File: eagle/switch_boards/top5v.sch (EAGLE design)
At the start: 9 parts

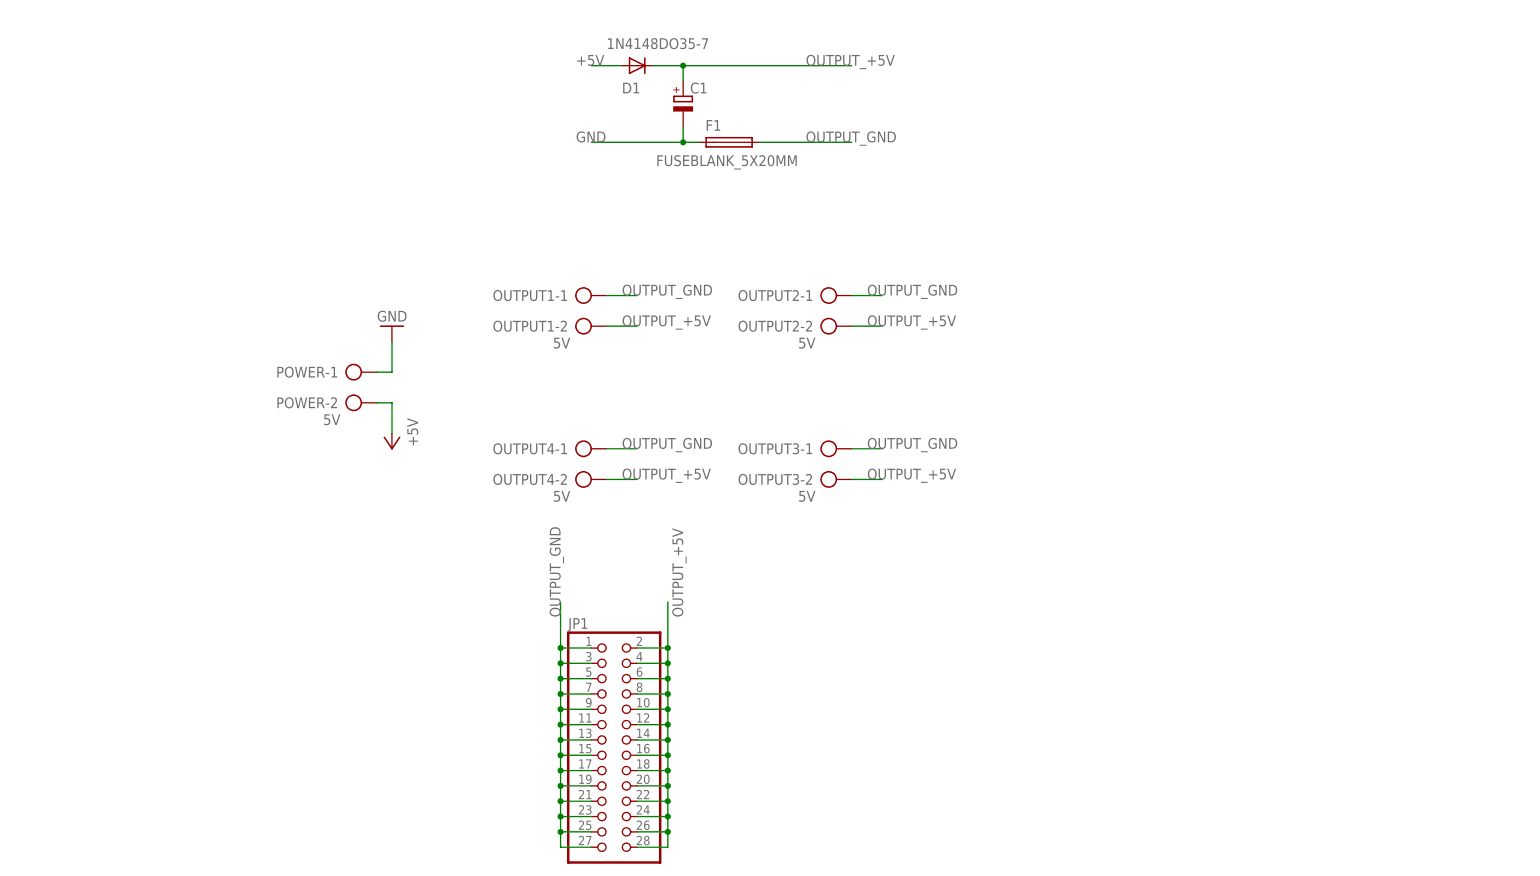
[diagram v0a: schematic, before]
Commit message: switch board for 5v
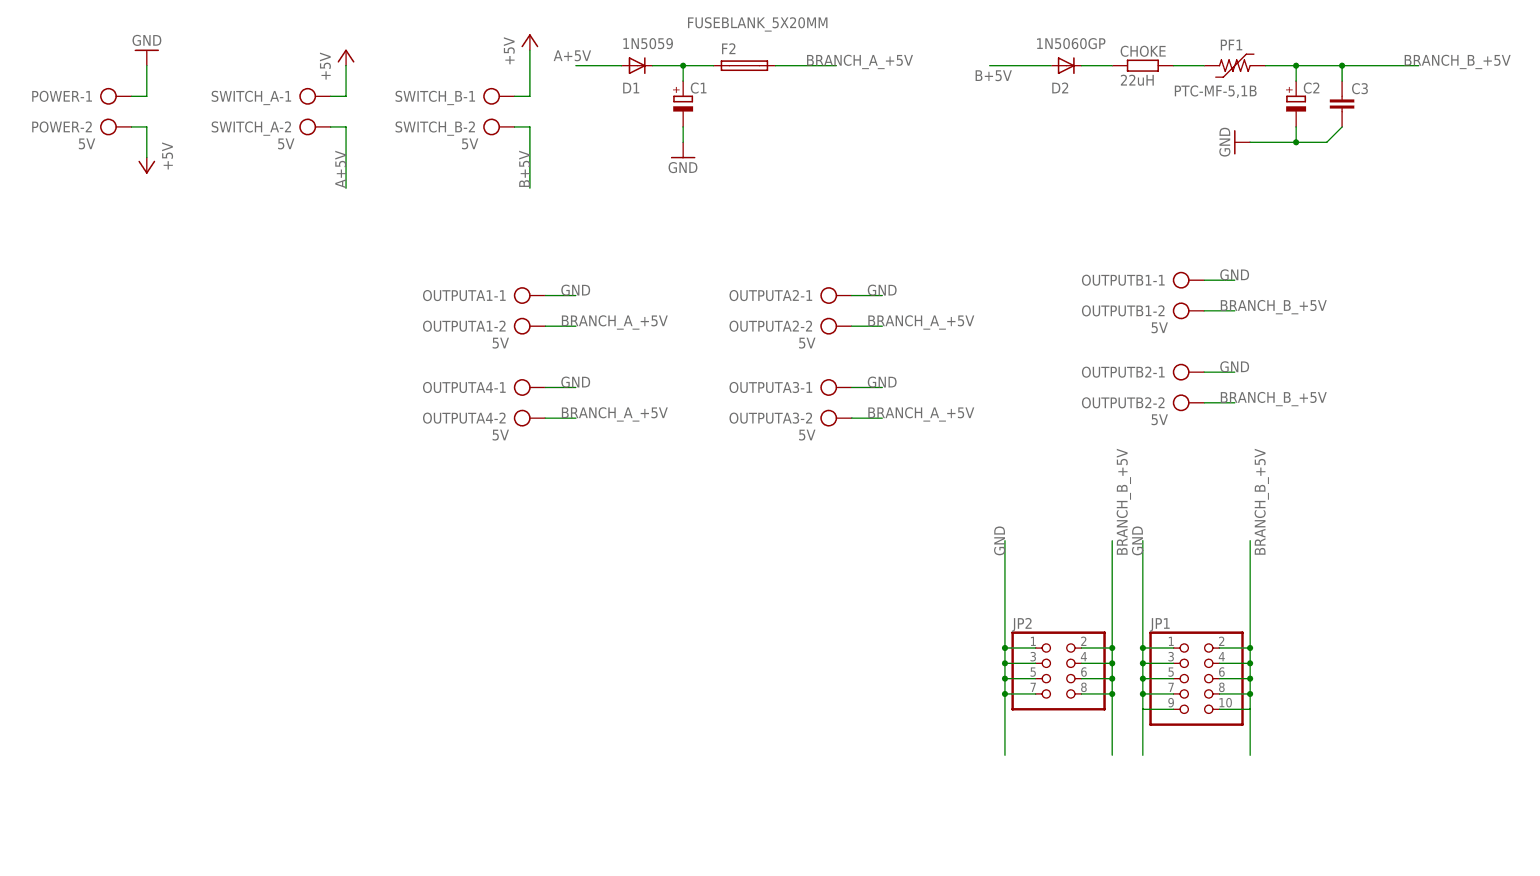
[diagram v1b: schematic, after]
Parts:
- removed F1: FUSEBLANK_5X20MM, fuse:FUSEBLANK_5X20MM
- removed OUTPUT1, OUTPUT2, OUTPUT3, OUTPUT4: 5V, con-ptr500:AK500/2-H
- added C2: (no value), rcl:CPOL-EUE2.5-5
- added C3: (no value), resistor:C-EU025-024X044
- added CHOKE: 22uH, resistor:R-EU_0411_15
- added D2: 1N5060GP, diode:1N5060GP
- added F2: FUSEBLANK_5X20MM, fuse:FUSEBLANK_5X20MM
- added JP2: (no value), pinhead:PINHD-2X4
- added OUTPUTA1, OUTPUTA2, OUTPUTA3, OUTPUTA4, OUTPUTB1, OUTPUTB2, SWITCH_A, SWITCH_B: 5V, con-ptr500:AK500/2
- added PF1: PTC-MF-5,1B, polyswitch:PTC-MF-5,1B
- C1: device resistor:CPOL-EUE1.8-4 -> rcl:CPOL-EUE2.5-5
- D1: value 1N4148DO35-7 -> 1N5059; device diode:1N4148DO35-7 -> diode:1N5059
- JP1: device pinhead:PINHD-2X14 -> pinhead:PINHD-2X5
- POWER: device con-ptr500:AK500/2-H -> con-ptr500:AK500/2
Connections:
- removed net OUTPUT_+5V: C1.+, D1.C, JP1.10, JP1.12, JP1.14, JP1.16, JP1.18, JP1.2, JP1.20, JP1.22, JP1.24, JP1.26, JP1.28, JP1.4, JP1.6, JP1.8, OUTPUT1-2.KL, OUTPUT2-2.KL, OUTPUT3-2.KL, OUTPUT4-2.KL
- removed net OUTPUT_GND: F1.1, JP1.1, JP1.11, JP1.13, JP1.15, JP1.17, JP1.19, JP1.21, JP1.23, JP1.25, JP1.27, JP1.3, JP1.5, JP1.7, JP1.9, OUTPUT1-1.KL, OUTPUT2-1.KL, OUTPUT3-1.KL, OUTPUT4-1.KL
- new net A+5V: D1.A, SWITCH_A-2.KL
- new net B+5V: D2.A, SWITCH_B-2.KL
- new net BRANCH_A_+5V: F2.1, OUTPUTA1-2.KL, OUTPUTA2-2.KL, OUTPUTA3-2.KL, OUTPUTA4-2.KL
- new net BRANCH_B_+5V: C2.+, C3.1, JP1.10, JP1.2, JP1.4, JP1.6, JP1.8, JP2.2, JP2.4, JP2.6, JP2.8, OUTPUTB1-2.KL, OUTPUTB2-2.KL, PF1.2
- new net N$1: CHOKE.1, D2.C
- new net N$12: C1.+, D1.C, F2.2
- new net N$2: CHOKE.2, PF1.1
- net +5V: now also SWITCH_A-1.KL, SWITCH_B-1.KL; no longer D1.A
- net GND: now also C2.-, C3.2, JP1.1, JP1.3, JP1.5, JP1.7, JP1.9, JP2.1, JP2.3, JP2.5, JP2.7, OUTPUTA1-1.KL, OUTPUTA2-1.KL, OUTPUTA3-1.KL, OUTPUTA4-1.KL, OUTPUTB1-1.KL, OUTPUTB2-1.KL; no longer F1.2
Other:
- moved on the sheet: POWER-1, POWER-2
